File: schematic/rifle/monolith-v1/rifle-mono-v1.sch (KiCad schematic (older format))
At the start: 75 parts, among them P1 MICROSD-SDIO-CD, P10 RC522, P11 Speaker1, P12 Speaker2, P13 I2C display, P14 I2C display, P15 FLASH, P16 VIBRO, P17 IR_LED, P18 USB_OTG, P19 GND, P2 SWD, P3 G B Vcc, P4 NRF24L01, P5 USB_A, P6 S_A_M1_M2, P7 DEBUG_TX, P8 Fire, P9 Reload, Q1 IRLML6402, Q2 IRLML2502, Q3 IRLML2502, Q4 IRLML2502, Q5 IRLML2502, Q6 IRLML2502, Q7 IRLML2502, U1 STM32F103RE, U2 USBLC6-4, U3 MCP73831, U4 NCP551, U5 PAM8403, Y1 8MHz

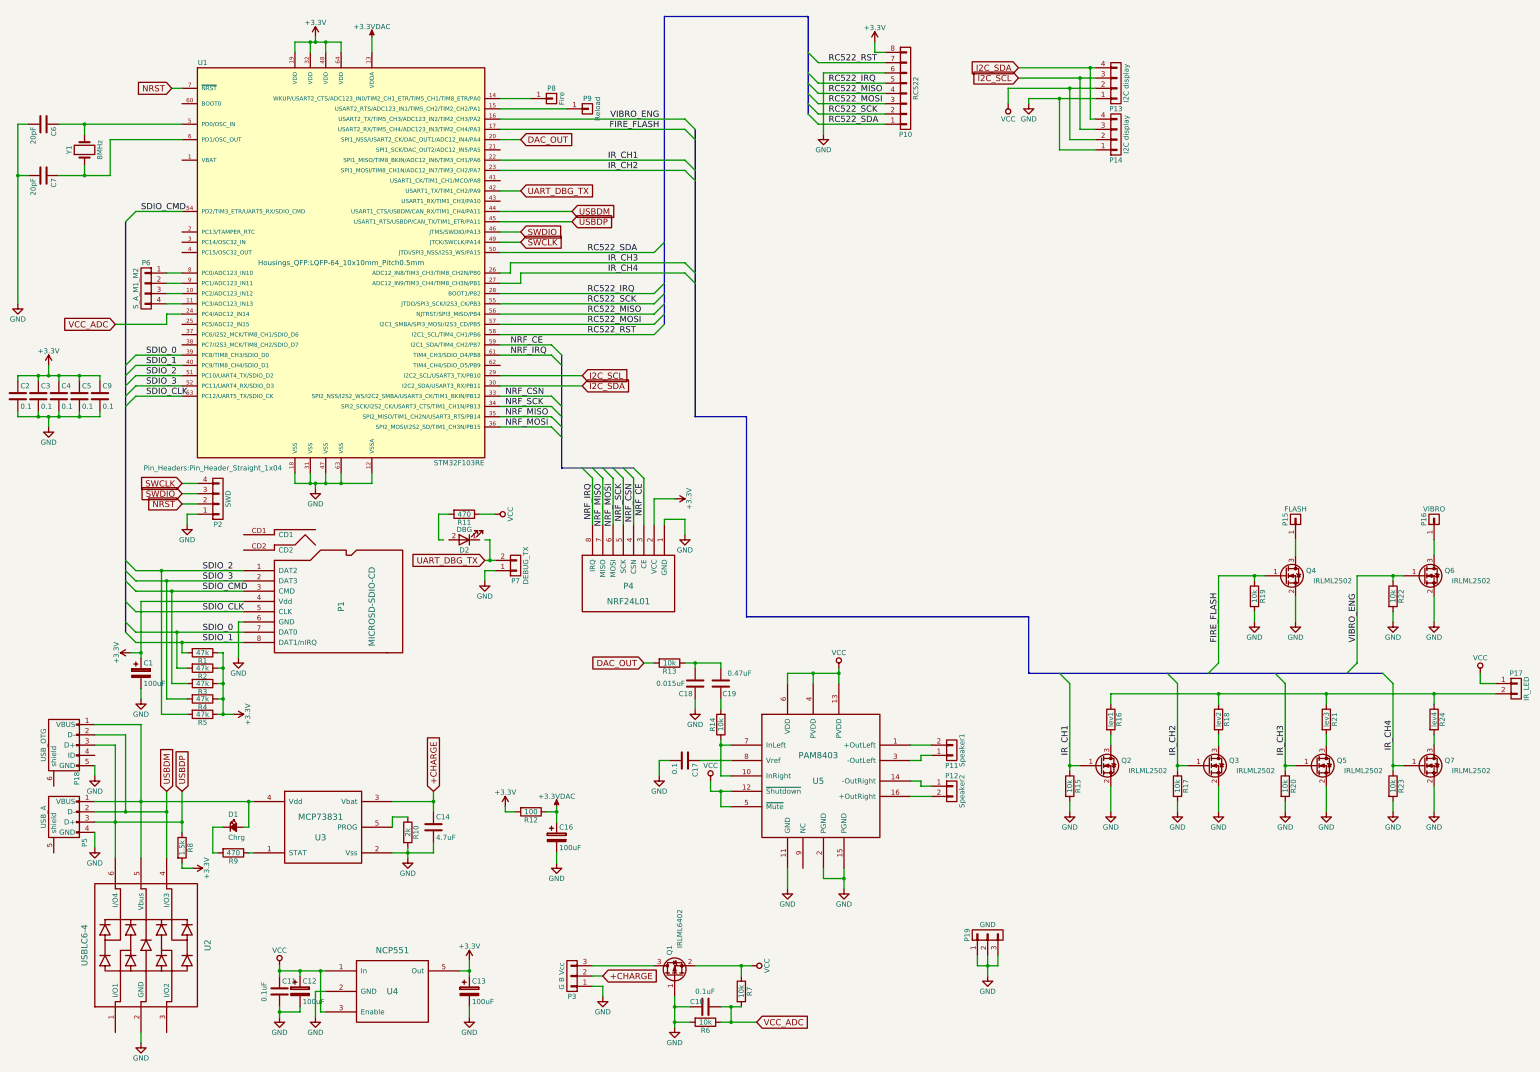
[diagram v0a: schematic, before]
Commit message: Rifle mono board 1.1: capacitor near PAM; I2C pull-up; Laser TTL output
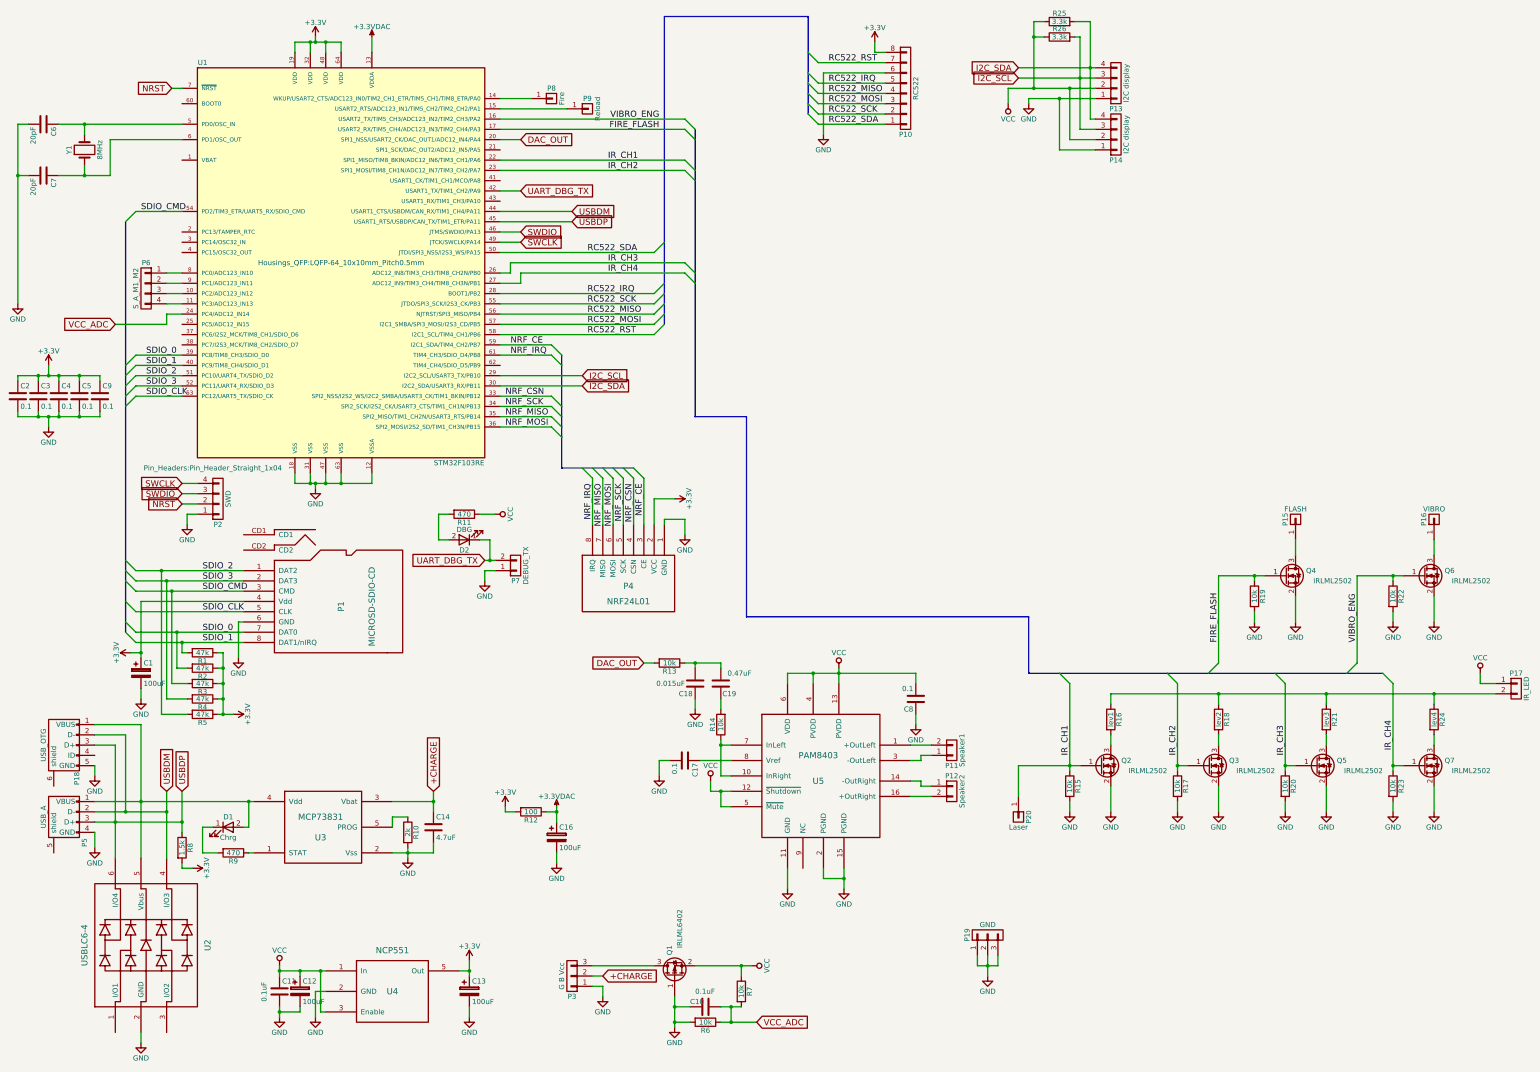
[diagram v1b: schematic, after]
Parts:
- removed D1: Chrg, LEDs:LED_0805, symbol Led_Small
- added C8: 0.1, Capacitors_SMD:C_0805, symbol C
- added D1: Chrg, LEDs:LED_0805, symbol LED
- added P20: Laser, Pin_Headers:Pin_Header_Straight_1x01_Pitch2.00mm, symbol CONN_01X01
- added R25, R26: 3.3k, Resistors_SMD:R_0805, symbol R
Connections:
- net GND: now also C8.1
- net I2C_SCL: now also R26.2
- net I2C_SDA: now also R25.2
- net IR_CH1: now also P20.1 (P1)
- net UART_DBG_TX: now also D2.1 (K)
- net VCC: now also C8.2, R25.1, R26.1
- net at P18.1 (VBUS), P5.1 (VBUS), U2.5 (Vbus)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: now also D1.2 (A)
- net at R9.2: now also D1.1 (K)
- net at D2.2 (A): now also R11.2
